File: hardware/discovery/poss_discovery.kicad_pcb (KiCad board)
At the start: 2 copper layers, 96.5 x 66 mm, 66 parts, among them CON1 USB-MICRO-B, SW1 SW_PUSH, SW10 SW_PUSH, SW11 SW_PUSH, SW12 SW_PUSH, SW13 SW_PUSH, SW14 SW_PUSH, SW15 SW_PUSH, SW16 SW_PUSH, SW17 SW_PUSH, SW18 SW_PUSH, SW19 SW_PUSH, SW2 SW_PUSH, SW20 SW_PUSH, SW21 SW_PUSH, SW22 SW_PUSH, SW3 SW_PUSH, SW4 SW_PUSH, SW5 SW_PUSH, SW6 SW_PUSH, SW7 SW_PUSH, SW8 SW_PUSH, SW9 SW_PUSH, U1 STM32F4_DISCO_Header, U2 MCP73831, U3 BD33IA5, U4 STM32F407VG

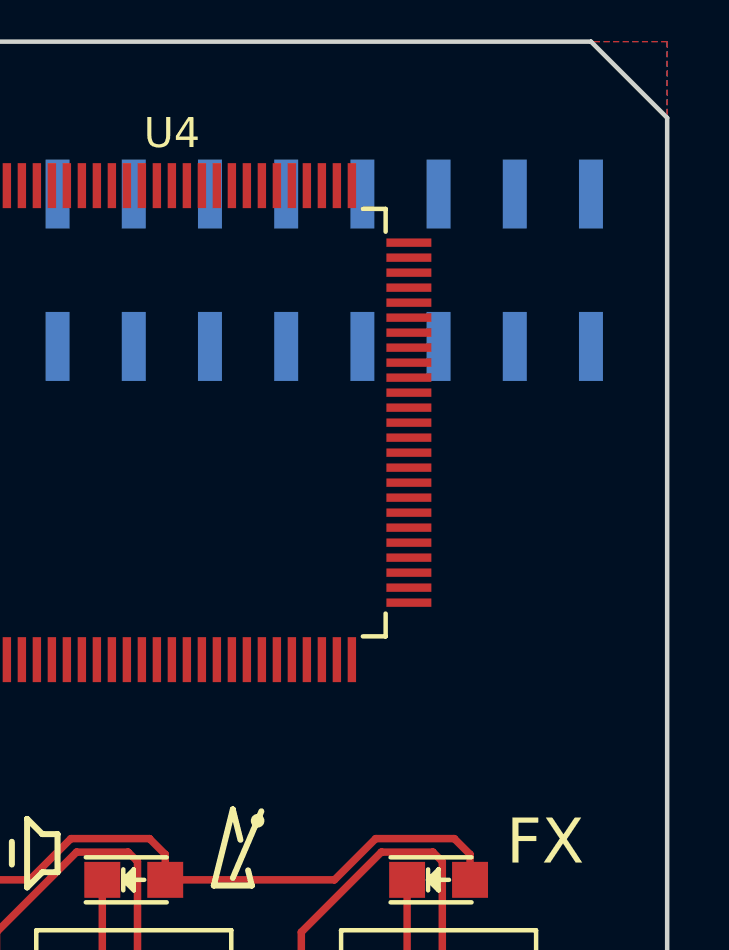
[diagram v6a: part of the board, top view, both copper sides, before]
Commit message: Discovery: SMT2F4 grounding
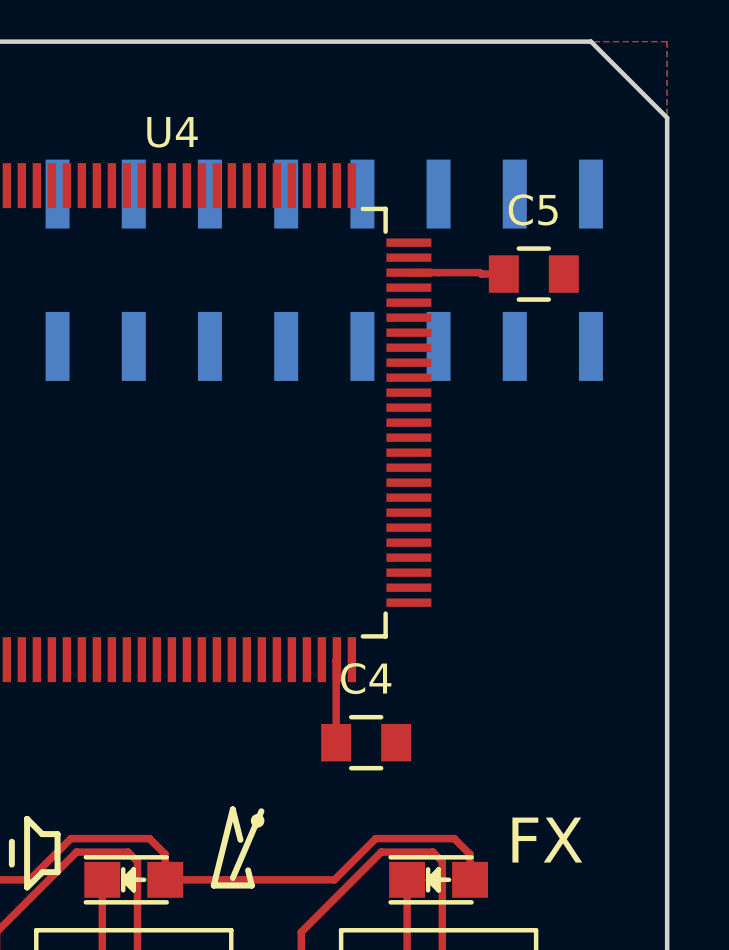
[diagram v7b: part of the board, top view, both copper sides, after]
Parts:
- added C4: 2.2uF, Capacitors_SMD:C_0805, F.Cu at (166.5, 102.1)
- added C5: 2.2uF, Capacitors_SMD:C_0805, F.Cu at (172.1, 86.5)
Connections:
- U4 pad 10: Net-(U4-Pad10) -> GND
- U4 pad 20: Net-(U4-Pad20) -> GND
- U4 pad 27: Net-(U4-Pad27) -> GND
- U4 pad 74: Net-(U4-Pad74) -> GND
- U4 pad 99: Net-(U4-Pad99) -> GND
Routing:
- net Net-(C5-Pad1): track 0.00 -> 3.18 mm
- net Net-(C4-Pad1): track 0.00 -> 2.78 mm

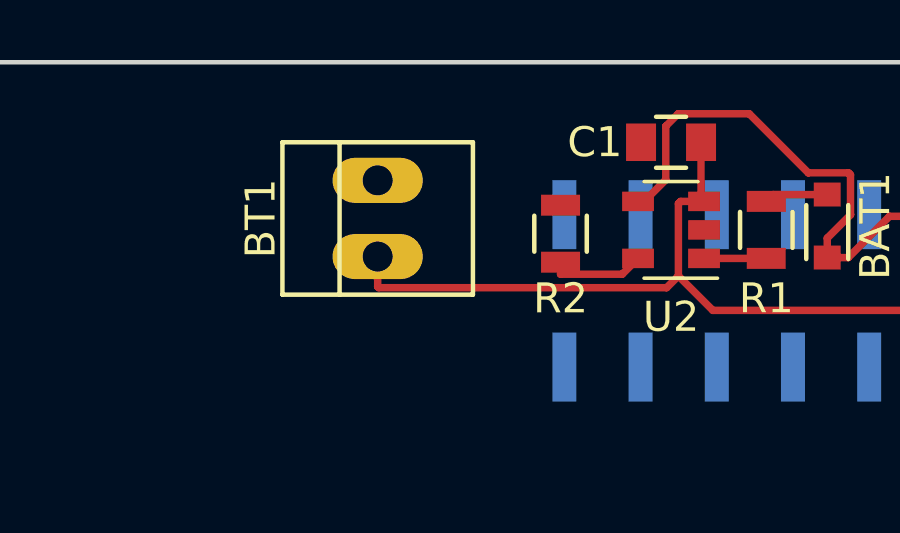
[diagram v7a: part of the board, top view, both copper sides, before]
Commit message: Discovery: Fix battery connector orientation
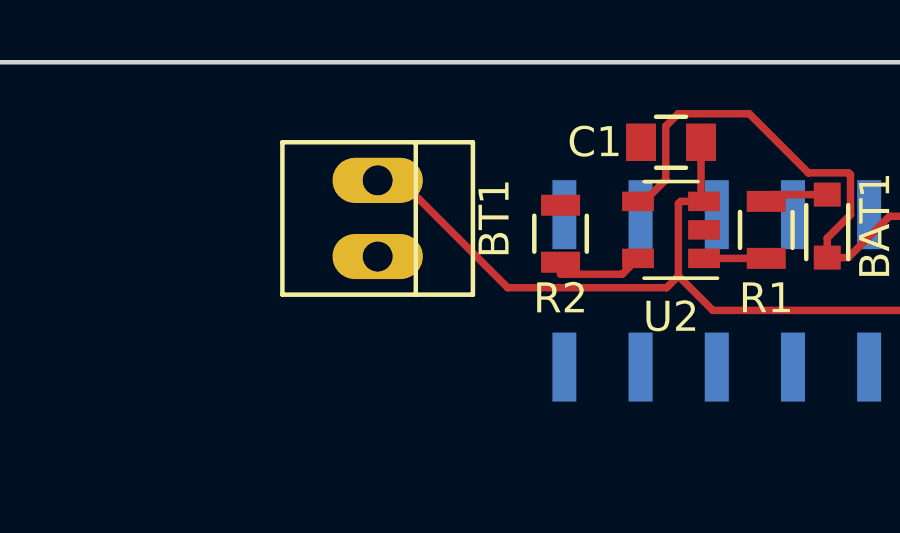
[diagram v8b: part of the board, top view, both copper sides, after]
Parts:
- turned BT1 to 270 degrees
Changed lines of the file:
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@@
     (add_net Write)
   )
+  (module Connect:PINHEAD1-2 (layer F.Cu)
+    (at 106.807 83.947 270)
+    (attr virtual)
+    (fp_text reference BT1 (at 0 -3.9 270) (layer F.SilkS)
+      (effects (font (size 1 1) (thickness 0.15)))
+    )
+    (fp_text value BATTERY (at 0 3.81 270) (layer F.Fab)
+      (effects (font (size 1 1) (thickness 0.15)))
+    )
+    (fp_line (start 2.54 -1.27) (end -2.54 -1.27) (layer F.SilkS) (width 0.15))
+    (fp_line (start 2.54 3.175) (end -2.54 3.175) (layer F.SilkS) (width 0.15))
+    (fp_line (start -2.54 -3.175) (end 2.54 -3.175) (layer F.SilkS) (width 0.15))
+    (fp_line (start -2.54 -3.175) (end -2.54 3.175) (layer F.SilkS) (width 0.15))
+    (fp_line (start 2.54 -3.175) (end 2.54 3.175) (layer F.SilkS) (width 0.15))
+    (pad 1 thru_hole oval (at -1.27 0 270) (size 1.50622 3.01498) (drill 0.99822) (layers *.Cu *.Mask)
+      (net 87 VBAT))
+    (pad 2 thru_hole oval (at 1.27 0 270) (size 1.50622 3.01498) (drill 0.99822) (layers *.Cu *.Mask)
+      (net 80 GND))
+  )
   (module Resistors_SMD:R_0805 (layer F.Cu)
     (at 119.761 84.328 90)
@@
     )
   )
-  (module Connect:PINHEAD1-2 (layer F.Cu)
-    (at 106.807 83.947 90)
-    (attr virtual)
-    (fp_text reference BT1 (at 0 -3.9 90) (layer F.SilkS)
-      (effects (font (size 1 1) (thickness 0.15)))
-    )
-    (fp_text value BATTERY (at 0 3.81 90) (layer F.Fab)
-      (effects (font (size 1 1) (thickness 0.15)))
-    )
-    (fp_line (start 2.54 -1.27) (end -2.54 -1.27) (layer F.SilkS) (width 0.15))
-    (fp_line (start 2.54 3.175) (end -2.54 3.175) (layer F.SilkS) (width 0.15))
-    (fp_line (start -2.54 -3.175) (end 2.54 -3.175) (layer F.SilkS) (width 0.15))
-    (fp_line (start -2.54 -3.175) (end -2.54 3.175) (layer F.SilkS) (width 0.15))
-    (fp_line (start 2.54 -3.175) (end 2.54 3.175) (layer F.SilkS) (width 0.15))
-    (pad 1 thru_hole oval (at -1.27 0 90) (size 1.50622 3.01498) (drill 0.99822) (layers *.Cu *.Mask)
-      (net 87 VBAT))
-    (pad 2 thru_hole oval (at 1.27 0 90) (size 1.50622 3.01498) (drill 0.99822) (layers *.Cu *.Mask)
-      (net 80 GND))
-  )
   (module Capacitors_SMD:C_0805 (layer F.Cu)
     (at 166.497 102.108)
@@
   (segment (start 145.4085 82.9235) (end 146.9485 82.9235) (width 0.25) (layer F.Cu) (net 80))
   (segment (start 119.761 85.278) (end 117.686 85.278) (width 0.25) (layer F.Cu) (net 86))
-  (segment (start 106.807 85.217) (end 106.807 86.22011) (width 0.25) (layer F.Cu) (net 87))
-  (segment (start 106.807 86.22011) (end 106.8419 86.25501) (width 0.25) (layer F.Cu) (net 87))
-  (segment (start 106.8419 86.25501) (end 116.43899 86.25501) (width 0.25) (layer F.Cu) (net 87))
+  (segment (start 116.43899 86.25501) (end 111.13939 86.25501) (width 0.25) (layer F.Cu) (net 87))
+  (segment (start 111.13939 86.25501) (end 107.56138 82.677) (width 0.25) (layer F.Cu) (net 87))
+  (segment (start 107.56138 82.677) (end 106.807 82.677) (width 0.25) (layer F.Cu) (net 87))
   (segment (start 116.43899 86.25501) (end 116.830999 85.863001) (width 0.25) (layer F.Cu) (net 87))
   (segment (start 127.828 87.011) (end 117.978998 87.011) (width 0.25) (layer F.Cu) (net 87))
